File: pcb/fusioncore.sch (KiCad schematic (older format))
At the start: 116 parts, among them J1 40HAT, J10 Pump_Misc_1, J11 Pump_Misc_2, J12 I2C_DBG, J13 Conn_02x03_Top_Bottom, J14 LED, J15 Trigger, J16 WEIGHT, J17 Valve_M1, J18 Valve_M2, J19 Valve_M3, J2 Conn_02x12_Top_Bottom, J20 Valve_M4, J21 Valve_Air_Lime, J22 Valve_Air_Rum, J23 Valve_Air_Out, J3 Flow_Warm, J4 Temperature, J5 Flow_Cold, J6 CONN_01X02, J7 Pump_Cold, J8 Pump_Warm, J9 Pump_Air, Q1 DMG2305UX, Q10 AO3400A, Q11 AO3400A, Q2 DMMT5401, Q3 AO3400A, Q4 AO3400A, Q5 AO3400A, Q6 AO3400A, Q7 AO3400A, Q8 MMBT4403, Q9 AO3400A, SW1 POWER_ON, U1 CAT24C32, U2 INA226, U3 INA226, U4 INA226, U5 TXB0108DQSR, U6 HX711, U7 P82B96

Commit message: Fixed issues from review.
Swapped diodes for Schottky diodes.
Changed logic level from HX711 to 3V3
Moved OE from 5V shifter to raspberry pi.
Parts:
- D10, D12, D16, D17, D18, D4, D6, D8: footprint Diode_SMD:D_SOD-123F -> Diode_SMD:D_SMA; LCSC C64898 -> C22452
- R1: value 150 -> 100; LCSC C17471 -> C17408
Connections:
- net labels added: EN_5V
- wire segments 481 -> 482
- no-connect marks 14 -> 13
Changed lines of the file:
@@
 Text Label 700  1550 0    50   ~ 0
 1W
-Text Notes 14400 3250 0    118  ~ 24
+Text Notes 14200 3250 0    118  ~ 24
 1 Wire Port
 $Comp
@@
 F 0 "D4" H 14750 5613 50  0000 C CNN
 F 1 "D_Small" H 14750 5614 50  0001 C CNN
-F 2 "Diode_SMD:D_SOD-123F" V 14750 5500 50  0001 C CNN
+F 2 "Diode_SMD:D_SMA" V 14750 5500 50  0001 C CNN
 F 3 "~" V 14750 5500 50  0001 C CNN
-F 4 "C64898" H 14750 5500 50  0001 C CNN "LCSC"
+F 4 "C22452" H 14750 5500 50  0001 C CNN "LCSC"
 	1    14750 5500
 	1    0    0    -1
@@
 F 0 "D6" H 14750 5913 50  0000 C CNN
 F 1 "D_Small" H 14750 5914 50  0001 C CNN
-F 2 "Diode_SMD:D_SOD-123F" V 14750 5800 50  0001 C CNN
+F 2 "Diode_SMD:D_SMA" V 14750 5800 50  0001 C CNN
 F 3 "~" V 14750 5800 50  0001 C CNN
-F 4 "C64898" H 14750 5800 50  0001 C CNN "LCSC"
+F 4 "C22452" H 14750 5800 50  0001 C CNN "LCSC"
 	1    14750 5800
 	1    0    0    -1
@@
 F 0 "D8" H 14750 6213 50  0000 C CNN
 F 1 "D_Small" H 14750 6214 50  0001 C CNN
-F 2 "Diode_SMD:D_SOD-123F" V 14750 6100 50  0001 C CNN
+F 2 "Diode_SMD:D_SMA" V 14750 6100 50  0001 C CNN
 F 3 "~" V 14750 6100 50  0001 C CNN
-F 4 "C64898" H 14750 6100 50  0001 C CNN "LCSC"
+F 4 "C22452" H 14750 6100 50  0001 C CNN "LCSC"
 	1    14750 6100
 	1    0    0    -1
@@
 F 0 "D10" H 14750 6513 50  0000 C CNN
 F 1 "D_Small" H 14750 6514 50  0001 C CNN
-F 2 "Diode_SMD:D_SOD-123F" V 14750 6400 50  0001 C CNN
+F 2 "Diode_SMD:D_SMA" V 14750 6400 50  0001 C CNN
 F 3 "~" V 14750 6400 50  0001 C CNN
-F 4 "C64898" H 14750 6400 50  0001 C CNN "LCSC"
+F 4 "C22452" H 14750 6400 50  0001 C CNN "LCSC"
 	1    14750 6400
 	1    0    0    -1
@@
 F 0 "D12" H 14750 6813 50  0000 C CNN
 F 1 "D_Small" H 14750 6814 50  0001 C CNN
-F 2 "Diode_SMD:D_SOD-123F" V 14750 6700 50  0001 C CNN
+F 2 "Diode_SMD:D_SMA" V 14750 6700 50  0001 C CNN
 F 3 "~" V 14750 6700 50  0001 C CNN
-F 4 "C64898" H 14750 6700 50  0001 C CNN "LCSC"
+F 4 "C22452" H 14750 6700 50  0001 C CNN "LCSC"
 	1    14750 6700
 	1    0    0    -1
@@
 F 0 "D18" V 10850 10468 50  0000 L CNN
 F 1 "D" V 10895 10468 50  0001 L CNN
-F 2 "Diode_SMD:D_SOD-123F" V 10850 10400 50  0001 C CNN
+F 2 "Diode_SMD:D_SMA" V 10850 10400 50  0001 C CNN
 F 3 "~" V 10850 10400 50  0001 C CNN
-F 4 "C64898" V 10850 10400 50  0001 C CNN "LCSC"
+F 4 "C22452" V 10850 10400 50  0001 C CNN "LCSC"
 	1    10850 10400
 	0    1    1    0
@@
 F 0 "D17" V 10500 10468 50  0000 L CNN
 F 1 "D" V 10545 10468 50  0001 L CNN
-F 2 "Diode_SMD:D_SOD-123F" V 10500 10400 50  0001 C CNN
+F 2 "Diode_SMD:D_SMA" V 10500 10400 50  0001 C CNN
 F 3 "~" V 10500 10400 50  0001 C CNN
-F 4 "C64898" V 10500 10400 50  0001 C CNN "LCSC"
+F 4 "C22452" V 10500 10400 50  0001 C CNN "LCSC"
 	1    10500 10400
 	0    1    1    0
@@
 F 0 "D16" V 10150 10468 50  0000 L CNN
 F 1 "D" V 10195 10468 50  0001 L CNN
-F 2 "Diode_SMD:D_SOD-123F" V 10150 10400 50  0001 C CNN
+F 2 "Diode_SMD:D_SMA" V 10150 10400 50  0001 C CNN
 F 3 "~" V 10150 10400 50  0001 C CNN
-F 4 "C64898" V 10150 10400 50  0001 C CNN "LCSC"
+F 4 "C22452" V 10150 10400 50  0001 C CNN "LCSC"
 	1    10150 10400
 	0    1    1    0
@@
 NoConn ~ 3100 2450
 NoConn ~ 3100 2350
-NoConn ~ 3100 1550
 Wire Wire Line
 	1900 2050 700  2050
@@
 P 12400 2050
 F 0 "R1" V 12300 2050 50  0000 C CNN
-F 1 "150" V 12400 2050 50  0000 C CNN
+F 1 "100" V 12400 2050 50  0000 C CNN
 F 2 "Resistor_SMD:R_0805_2012Metric_Pad1.15x1.40mm_HandSolder" V 12330 2050 50  0001 C CNN
 F 3 "~" H 12400 2050 50  0001 C CNN
-F 4 "C17471" V 12400 2050 50  0001 C CNN "LCSC"
+F 4 "C17408" V 12400 2050 50  0001 C CNN "LCSC"
 	1    12400 2050
 	0    1    1    0
@@
 Wire Wire Line
 	6800 8700 7200 8700
-Connection ~ 6800 8700
-Text Label 7100 8700 0    50   ~ 0
+Text Label 5400 8700 2    50   ~ 0
 5V
 $Comp
@@
 Wire Wire Line
 	5150 9050 5150 8900
-Connection ~ 5150 8700
-Wire Wire Line
-	5150 8700 6800 8700
 Wire Wire Line
 	5150 8900 4800 8900
@@
 NoConn ~ 3100 2750
 NoConn ~ 3100 2950
-$Comp
-L Logic_LevelTranslator:TXB0108DQSR U5
-U 1 1 5E397B97
-P 1400 6950
-F 0 "U5" H 1400 6161 50  0000 C CNN
-F 1 "TXB0108DQSR" H 1400 6070 50  0000 C CNN
-F 2 "Package_SO:TSSOP-20_4.4x6.5mm_P0.65mm" H 1400 6200 50  0001 C CNN
-F 3 "http://www.ti.com/lit/ds/symlink/txb0108.pdf" H 1400 6850 50  0001 C CNN
-F 4 "C53406" H 1400 6950 50  0001 C CNN "LCSC"
-	1    1400 6950
-	1    0    0    -1
-$EndComp
 Wire Wire Line
 	1300 6250 1300 5900
@@
 $EndComp
 Wire Wire Line
-	1300 6250 1000 6250
-Wire Wire Line
 	1000 6250 1000 6550
-Connection ~ 1300 6250
 $Comp
 L power:GND #PWR018
@@
 	0    -1   -1   0
 $EndComp
-Connection ~ 1000 6250
 Wire Notes Line
 	2650 7250 4400 7250
@@
 	10200 2750 10350 2750
 NoConn ~ 15450 1550
+Wire Wire Line
+	5150 8700 5400 8700
+Connection ~ 5150 8700
+Text Label 7200 8700 2    50   ~ 0
+3V3
+$Comp
+L Logic_LevelTranslator:TXB0108DQSR U5
+U 1 1 5E397B97
+P 1400 6950
+F 0 "U5" H 1400 6161 50  0000 C CNN
+F 1 "TXB0108DQSR" H 1400 6070 50  0000 C CNN
+F 2 "Package_SO:TSSOP-20_4.4x6.5mm_P0.65mm" H 1400 6200 50  0001 C CNN
+F 3 "http://www.ti.com/lit/ds/symlink/txb0108.pdf" H 1400 6850 50  0001 C CNN
+F 4 "C53406" H 1400 6950 50  0001 C CNN "LCSC"
+	1    1400 6950
+	1    0    0    -1
+$EndComp
+Wire Wire Line
+	1000 6250 1000 5900
+Connection ~ 1000 6250
+Text Label 1000 5900 3    50   ~ 0
+EN_5V
+Wire Wire Line
+	3100 1550 4300 1550
+Text Label 4300 1550 2    50   ~ 0
+EN_5V
 $EndSCHEMATC

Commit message: Simplified the EEPROM by removing an unecessary jumper
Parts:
- removed J6: CONN_01X02, Connector_PinHeader_2.54mm:PinHeader_1x02_P2.54mm_Vertical, symbol Connector_Generic:Conn_01x02
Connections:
- wire segments 482 -> 474
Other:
- moved on the sheet: JP2, R15
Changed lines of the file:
@@
 	2500 4700 2750 4700
-$Comp
-L Connector_Generic:Conn_01x02 J6
-U 1 1 58E18D32
-P 650 4850
-F 0 "J6" H 650 5000 50  0000 C CNN
-F 1 "CONN_01X02" V 750 4850 50  0000 C CNN
-F 2 "Connector_PinHeader_2.54mm:PinHeader_1x02_P2.54mm_Vertical" H 650 4850 50  0001 C CNN
-F 3 "" H 650 4850 50  0000 C CNN
-	1    650  4850
-	-1   0    0    1
-$EndComp
 $Comp
 L Device:R R15
 U 1 1 58E19E51
-P 1450 5000
-F 0 "R15" V 1530 5000 50  0000 C CNN
-F 1 "10K" V 1450 5000 50  0000 C CNN
-F 2 "Resistor_SMD:R_0805_2012Metric_Pad1.15x1.40mm_HandSolder" V 1380 5000 50  0001 C CNN
-F 3 "" H 1450 5000 50  0001 C CNN
-F 4 "C17414" V 1450 5000 50  0001 C CNN "LCSC"
-	1    1450 5000
-	-1   0    0    1
+P 900 4800
+F 0 "R15" V 980 4800 50  0000 C CNN
+F 1 "10K" V 900 4800 50  0000 C CNN
+F 2 "Resistor_SMD:R_0805_2012Metric_Pad1.15x1.40mm_HandSolder" V 830 4800 50  0001 C CNN
+F 3 "" H 900 4800 50  0001 C CNN
+F 4 "C17414" V 900 4800 50  0001 C CNN "LCSC"
+	1    900  4800
+	0    1    1    0
 $EndComp
 Text Label 2300 4100 2    60   ~ 0
@@
 Wire Wire Line
 	1200 4600 1500 4600
-$Comp
-L power:GND #PWR012
-U 1 1 58E1AF98
-P 950 4900
-F 0 "#PWR012" H 950 4650 50  0001 C CNN
-F 1 "GND" H 950 4750 50  0000 C CNN
-F 2 "" H 950 4900 50  0000 C CNN
-F 3 "" H 950 4900 50  0000 C CNN
-	1    950  4900
-	1    0    0    -1
-$EndComp
 Text Notes 1900 3550 0    118  ~ 24
 HAT EEPROM
@@
 Wire Wire Line
 	2000 5000 2000 5100
-Text Label 1700 5300 2    60   ~ 0
+Text Label 650  5150 1    60   ~ 0
 3V3_PI
-Wire Wire Line
-	1700 5300 1450 5300
-Wire Wire Line
-	1450 5300 1450 5150
-Wire Wire Line
-	1350 4800 1450 4800
-Wire Wire Line
-	1450 4750 1450 4800
 Wire Wire Line
 	950  4400 950  4500
 Connection ~ 1200 4400
 Wire Wire Line
-	1350 4800 1350 4850
-Connection ~ 1450 4800
-Wire Wire Line
-	850  4850 950  4850
-Wire Wire Line
-	950  4900 950  4850
-Connection ~ 950  4850
-Wire Wire Line
-	850  4750 1450 4750
-Wire Wire Line
 	6550 2550 6550 2700
 Wire Wire Line
@@
 Wire Wire Line
 	1200 4400 1500 4400
-Wire Wire Line
-	1450 4800 1500 4800
-Wire Wire Line
-	1450 4800 1450 4850
-Wire Wire Line
-	950  4850 1050 4850
 Text Label 12650 1350 0    50   ~ 0
 3V3_ATX
@@
 L Jumper:SolderJumper_2_Open JP2
 U 1 1 5ED7B1E0
-P 1200 4850
-F 0 "JP2" H 1200 4750 50  0000 C CNN
-F 1 "SolderJumper_2_Open" H 1200 4964 50  0001 C CNN
-F 2 "Jumper:SolderJumper-2_P1.3mm_Open_Pad1.0x1.5mm" H 1200 4850 50  0001 C CNN
-F 3 "~" H 1200 4850 50  0001 C CNN
-	1    1200 4850
+P 1200 4800
+F 0 "JP2" H 1200 4700 50  0000 C CNN
+F 1 "SolderJumper_2_Open" H 1200 4914 50  0001 C CNN
+F 2 "Jumper:SolderJumper-2_P1.3mm_Open_Pad1.0x1.5mm" H 1200 4800 50  0001 C CNN
+F 3 "~" H 1200 4800 50  0001 C CNN
+	1    1200 4800
 	1    0    0    -1
 $EndComp
@@
 Text Label 4300 1550 2    50   ~ 0
 EN_5V
+Wire Wire Line
+	750  4800 650  4800
+Wire Wire Line
+	1350 4800 1500 4800
+Wire Wire Line
+	650  4800 650  5150
 $EndSCHEMATC

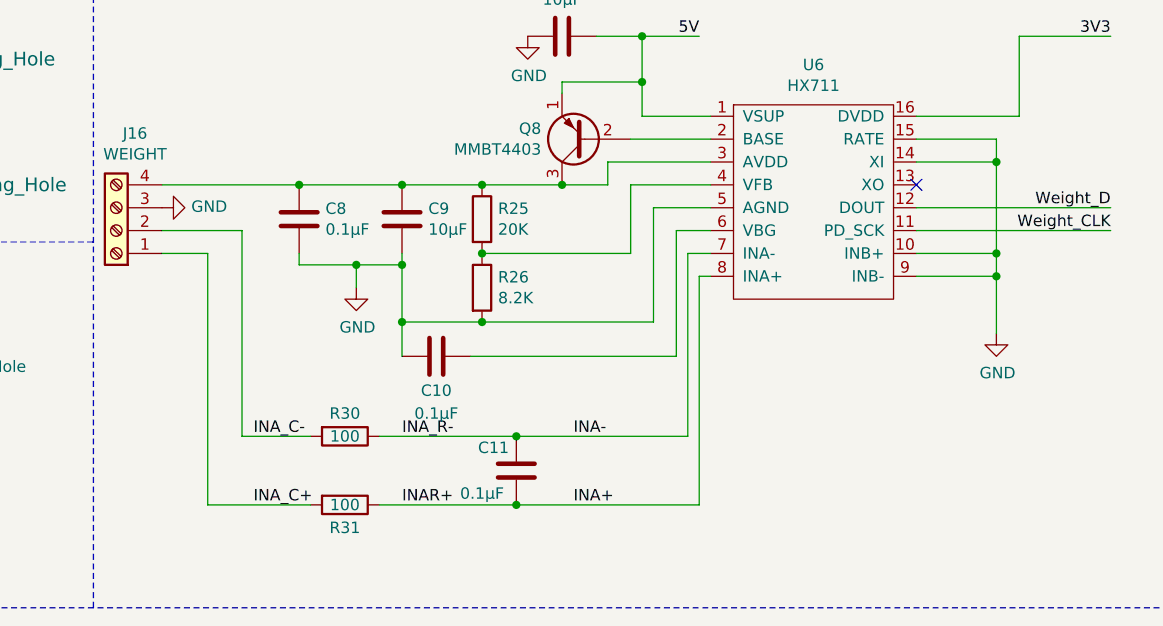
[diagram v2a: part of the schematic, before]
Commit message: Added B+/- weight connector
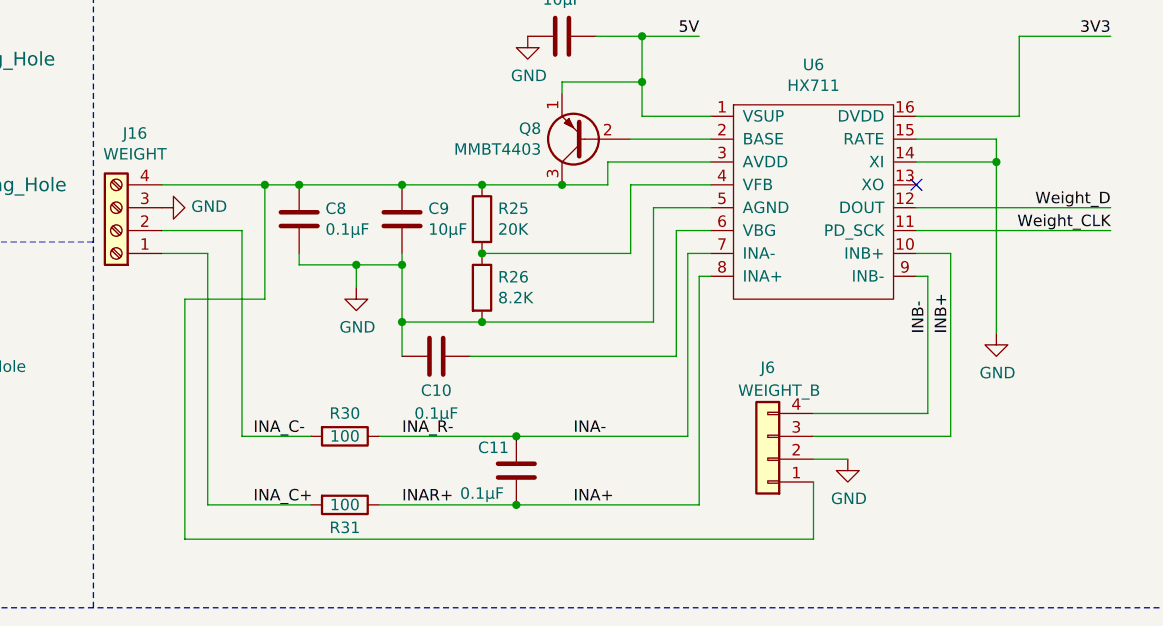
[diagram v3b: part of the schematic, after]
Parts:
- added J6: WEIGHT_B, Connector_PinHeader_2.54mm:PinHeader_1x04_P2.54mm_Vertical, symbol Connector_Generic:Conn_01x04
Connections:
- net GND: now also J6.2 (Pin_2); no longer U6.10 (INB+), U6.9 (INB-)
- net at C8.2, C9.2, J16.4 (Pin_4)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: now also J6.1 (Pin_1)
- new net INB+: J6.3 (Pin_3), U6.10 (INB+)
- new net INB-: J6.4 (Pin_4), U6.9 (INB-)
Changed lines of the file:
@@
 	6350 9250 6700 9250
 Connection ~ 6700 9250
-Wire Wire Line
-	6700 9250 6700 9650
-Wire Wire Line
-	6350 9650 6700 9650
-Connection ~ 6700 9650
-Wire Wire Line
-	6700 9650 6700 9750
-Wire Wire Line
-	6350 9750 6700 9750
-Connection ~ 6700 9750
-Wire Wire Line
-	6700 9750 6700 10000
 $Comp
 L power:GND #PWR027
@@
 	0    -1   -1   0
 $EndComp
-Wire Wire Line
-	3050 9350 3650 9350
 Connection ~ 4100 9350
 Wire Wire Line
@@
 Wire Wire Line
 	650  4800 650  5150
+Wire Wire Line
+	6700 9250 6700 10000
+Wire Wire Line
+	6350 9750 6400 9750
+Wire Wire Line
+	6350 9650 6500 9650
+Text Label 6400 10000 1    50   ~ 0
+INB-
+Text Label 6500 10000 1    50   ~ 0
+INB+
+$Comp
+L Connector_Generic:Conn_01x04 J6
+U 1 1 5E5CE1FB
+P 5700 10550
+F 0 "J6" H 5700 10150 50  0000 C CNN
+F 1 "WEIGHT_B" H 5650 10250 50  0000 C CNN
+F 2 "Connector_PinHeader_2.54mm:PinHeader_1x04_P2.54mm_Vertical" H 5700 10550 50  0001 C CNN
+F 3 "" H 5700 10550 50  0000 C CNN
+	1    5700 10550
+	-1   0    0    1
+$EndComp
+Wire Wire Line
+	3150 10900 5900 10900
+Wire Wire Line
+	5900 10900 5900 10650
+Wire Wire Line
+	6400 9750 6400 10350
+Wire Wire Line
+	6400 10350 5900 10350
+Wire Wire Line
+	6500 10450 5900 10450
+Wire Wire Line
+	6500 9650 6500 10450
+$Comp
+L power:GND #PWR012
+U 1 1 5E776A6B
+P 6050 10550
+F 0 "#PWR012" H 6050 10300 50  0001 C CNN
+F 1 "GND" H 6055 10377 50  0000 C CNN
+F 2 "" H 6050 10550 50  0001 C CNN
+F 3 "" H 6050 10550 50  0001 C CNN
+	1    6050 10550
+	1    0    0    -1
+$EndComp
+Wire Wire Line
+	5900 10550 6050 10550
+Wire Wire Line
+	3050 9350 3500 9350
+Wire Wire Line
+	3500 9350 3500 9850
+Wire Wire Line
+	3500 9850 3150 9850
+Wire Wire Line
+	3150 9850 3150 10900
+Connection ~ 3500 9350
+Wire Wire Line
+	3500 9350 3650 9350
 $EndSCHEMATC
